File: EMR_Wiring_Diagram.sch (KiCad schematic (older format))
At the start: 22 parts, among them SW1 Ignition_SWT, SW2 PRCHRG_SWT

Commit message: moved some stuff added contractor
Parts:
- added U?: Line_contactor, symbol Line_contactor
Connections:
- net 12V: now also U?.2 (V+)
- net GND: now also SWI3.2
- net bat_bms/BAT+: now also U?.4 (Vout); no longer SWI4.2
- net bat_bms/BAT-: no longer U?.S2 (IGNITION_GND)
- net at 4A.1, 800A.1: now also U?.3 (Vin); no longer SWI3.2
- new net: SWI4.2, U?.1 (V-)
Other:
- moved on the sheet: 4A, 800A, Brake, D1, D2, Precharge, R1, R2, SP1, SW1, SW2, SWI1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

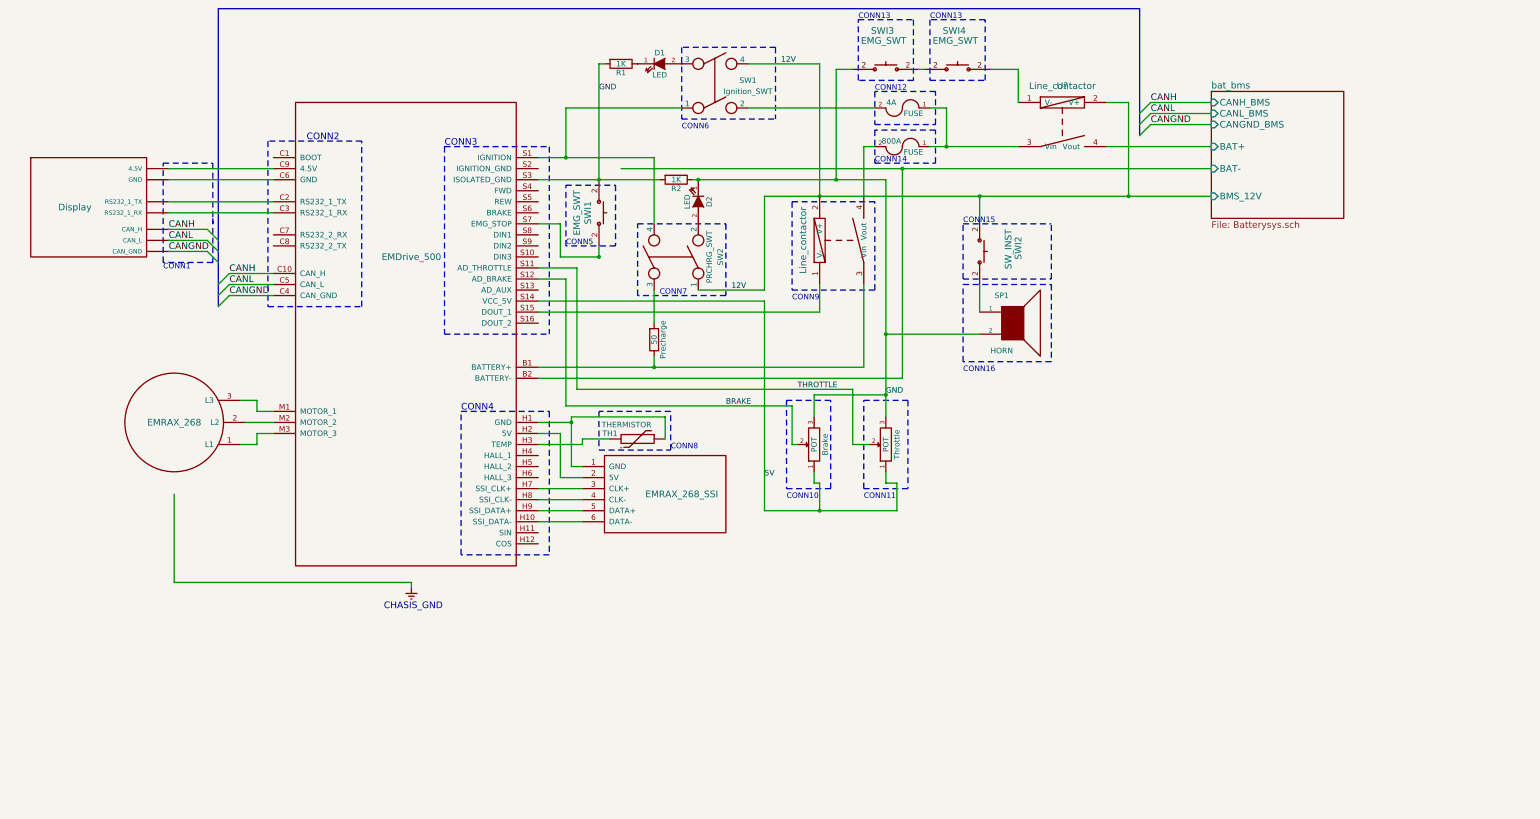
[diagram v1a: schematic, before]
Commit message: Finalized Diagram
Combined Emergency Switches, adjusted recharge loop, labeled wires and
wire colors, adjusted connection labels to match the list that Connor
made.
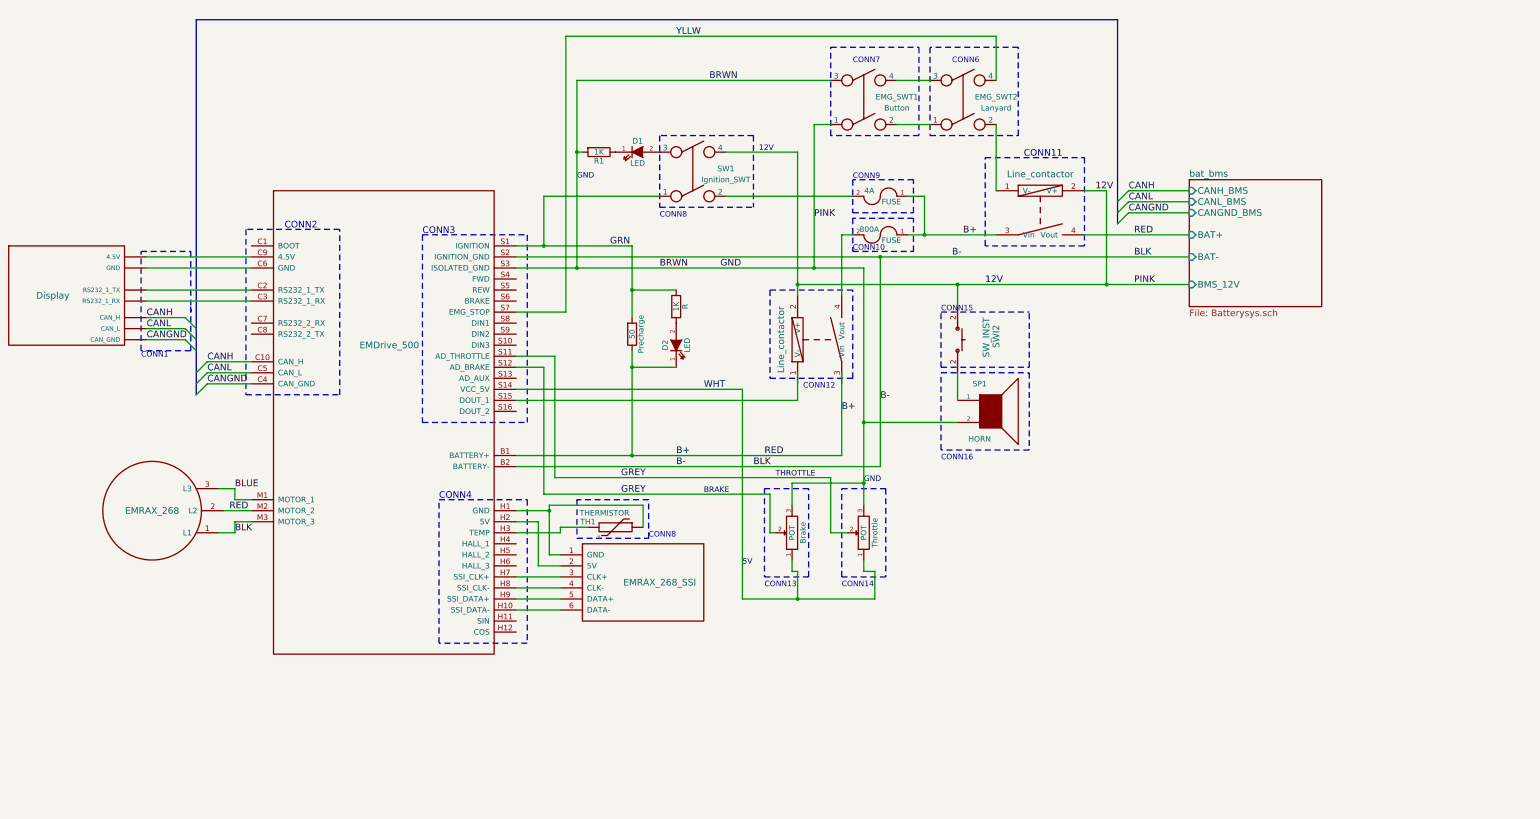
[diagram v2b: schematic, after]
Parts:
- removed R2: 1K, symbol R
- removed SW2: PRCHRG_SWT, symbol Switch_DPST
- removed SWI1, SWI3, SWI4: EMG_SWT, symbol SW_INST
- added EMG_SWT1: Button, symbol Switch_DPST
- added EMG_SWT2: Lanyard, symbol Switch_DPST
- added R: 1K, symbol R
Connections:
- net THROTTLE is gone; now on net BRAKE: Throttle.2, U?.S11 (AD_THROTTLE)
- net bat_bms/BAT+ is gone; now on net B+: U?.4 (Vout)
- net bat_bms/BAT- is gone; now on net B-: U?.B2 (BATTERY-)
- net 12V: now also Brake.3, R1.2, SP1.2, Throttle.3, U?.S3 (ISOLATED_GND), EMG_SWT1.1, EMG_SWT1.3
- net B+: now reaches Precharge.1, U?.B1 (BATTERY+)
- net B+: now also 4A.1, 800A.1, D2.1 (K), U?.2 (L2), U?.3 (Vin), U?.M2 (MOTOR_2); no longer U?.3 (Vin)
- net BLUE: now reaches U?.3 (L3), U?.M1 (MOTOR_1)
- net B-: now reaches U?.1 (L1), U?.M3 (MOTOR_3)
- net B-: now also U?.S2 (IGNITION_GND)
- net GRN: now reaches SW1.1, U?.S1 (IGNITION)
- net GRN: now also Precharge.2, R.1
- net at U?.S15 (DOUT_1): no longer U?.1 (V-)
- net YLLW: now reaches U?.S7 (EMG_STOP)
- net YLLW: now also EMG_SWT2.4
- net at D2.2 (A): now also R.2
- net at U?.1 (V-): now also EMG_SWT2.2
- removed net GND: Brake.3, D2.1 (K), R1.2, SP1.2, Throttle.3, U?.S3 (ISOLATED_GND)
- new net: EMG_SWT1.2, EMG_SWT2.1
- new net: EMG_SWT1.4, EMG_SWT2.3
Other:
- note added: "CONN11"
- note added: "CONN14"
- note added: "CONN6\n"
- note removed: "CHASIS_GND\n"
- note removed: "CONN11\n"
- note removed: "CONN13"
- note removed: "CONN14\n"
- note removed: "CONN5"
- note removed: "CONN6"
- moved on the sheet: 4A, 800A, Brake, D1, Precharge, R1, SP1, SW1, SWI2, TH1, Throttle

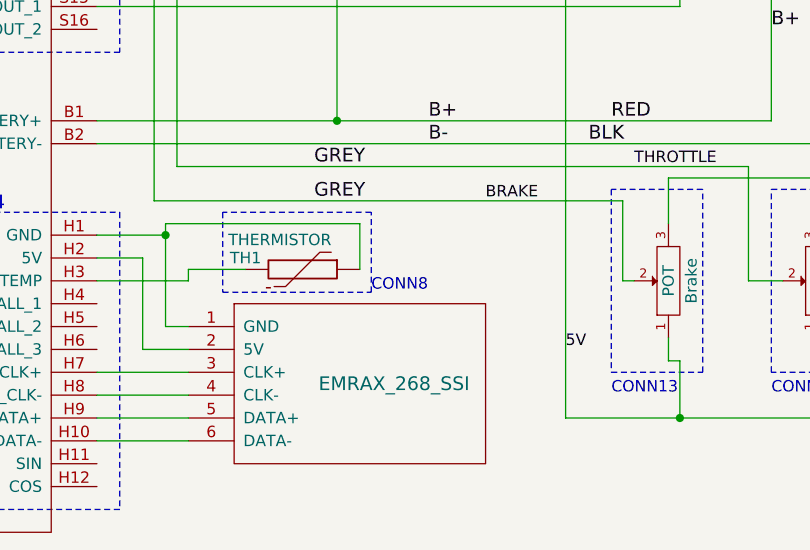
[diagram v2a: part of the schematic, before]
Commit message: Changed thermistor connector #
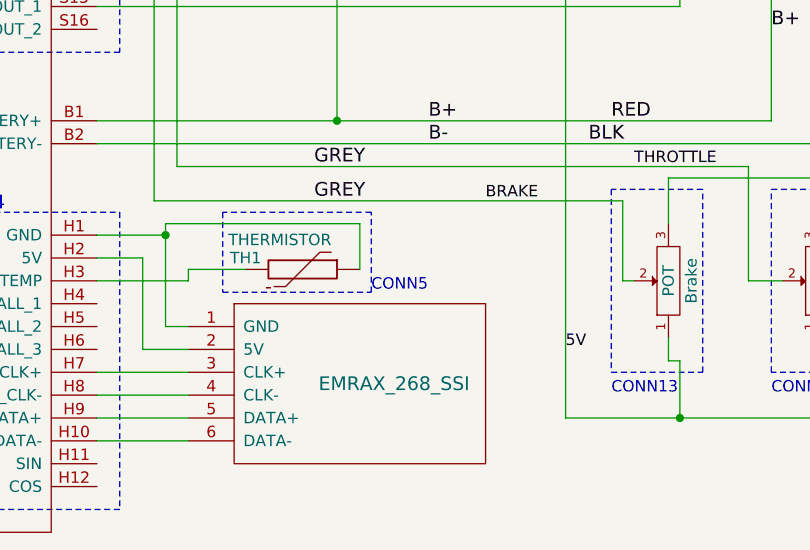
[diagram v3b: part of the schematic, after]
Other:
- note added: "CONN5\n"
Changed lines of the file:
@@
 CONN15\n
 Text Notes 6450 5450 0    50   ~ 0
-CONN8
+CONN5\n
 $Comp
 L Line_contactor U?
